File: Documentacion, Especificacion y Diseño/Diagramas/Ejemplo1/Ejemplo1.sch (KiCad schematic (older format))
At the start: 12 parts

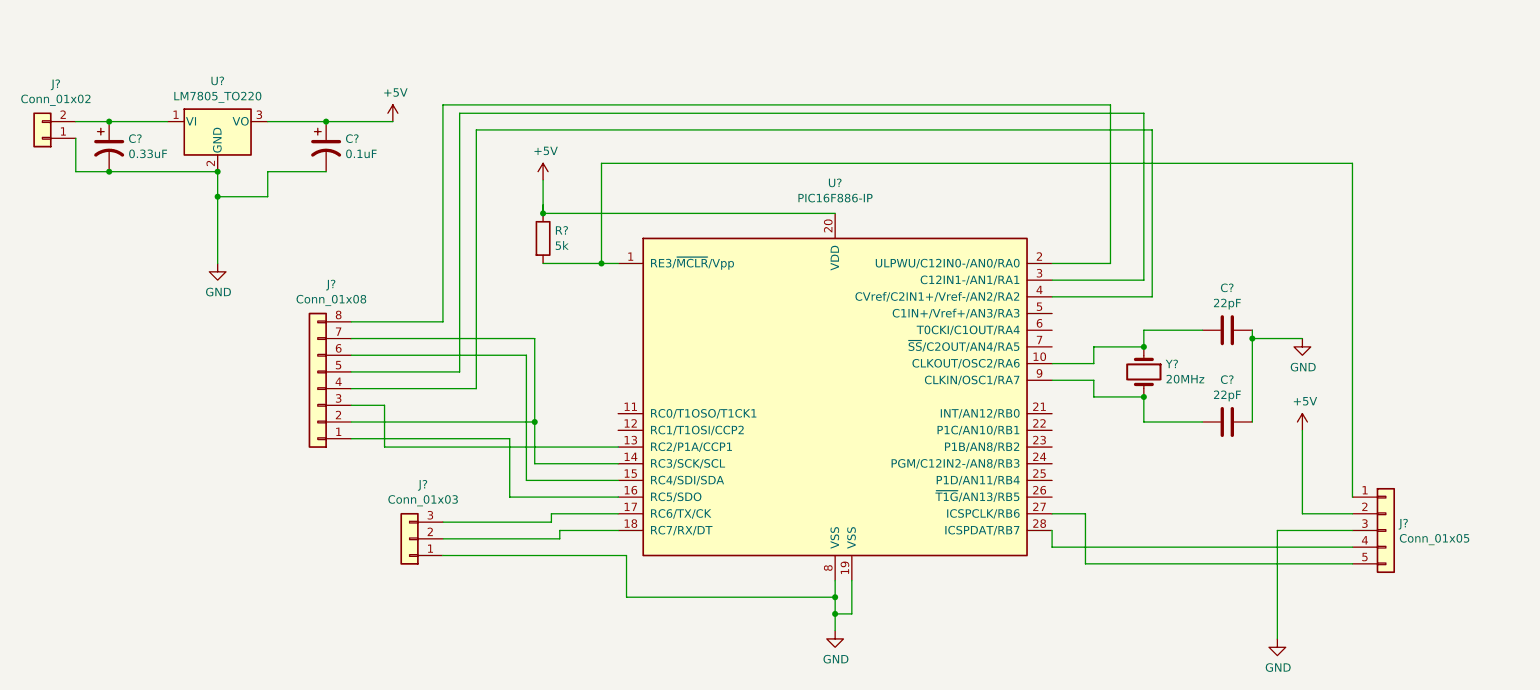
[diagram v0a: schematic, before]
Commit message: Tratado de hacer parte del circuito sin cruces y con especificaciones
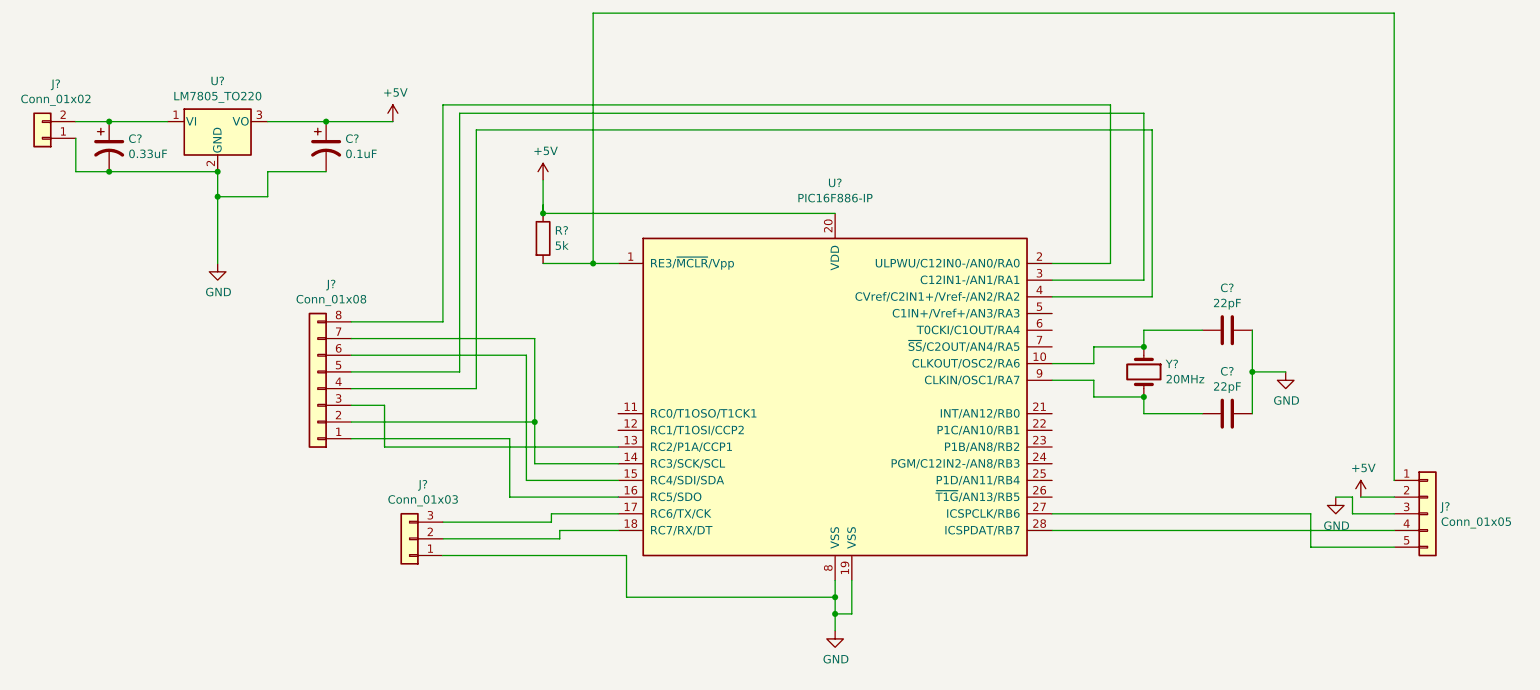
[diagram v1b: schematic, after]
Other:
- moved on the sheet: C?, J?
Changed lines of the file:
@@
 $EndComp
-Wire Wire Line
-	4000 2850 4350 2850
 Wire Wire Line
 	5750 2550 4000 2550
@@
 L Connector_Generic:Conn_01x05 J?
 U 1 1 635B6CD0
-P 9050 4450
-F 0 "J?" H 9130 4492 50  0000 L CNN
-F 1 "Conn_01x05" H 9130 4401 50  0000 L CNN
-F 2 "" H 9050 4450 50  0001 C CNN
-F 3 "~" H 9050 4450 50  0001 C CNN
-	1    9050 4450
+P 9300 4350
+F 0 "J?" H 9380 4392 50  0000 L CNN
+F 1 "Conn_01x05" H 9380 4301 50  0000 L CNN
+F 2 "" H 9300 4350 50  0001 C CNN
+F 3 "~" H 9300 4350 50  0001 C CNN
+	1    9300 4350
 	1    0    0    -1
 $EndComp
@@
 L power:+5V #PWR?
 U 1 1 635C3E4F
-P 8550 3850
-F 0 "#PWR?" H 8550 3700 50  0001 C CNN
-F 1 "+5V" H 8565 4023 50  0000 C CNN
-F 2 "" H 8550 3850 50  0001 C CNN
-F 3 "" H 8550 3850 50  0001 C CNN
-	1    8550 3850
+P 8900 4250
+F 0 "#PWR?" H 8900 4100 50  0001 C CNN
+F 1 "+5V" H 8915 4423 50  0000 C CNN
+F 2 "" H 8900 4250 50  0001 C CNN
+F 3 "" H 8900 4250 50  0001 C CNN
+	1    8900 4250
 	1    0    0    -1
 $EndComp
@@
 L power:GND #PWR?
 U 1 1 635C471C
-P 8400 5100
-F 0 "#PWR?" H 8400 4850 50  0001 C CNN
-F 1 "GND" H 8405 4927 50  0000 C CNN
-F 2 "" H 8400 5100 50  0001 C CNN
-F 3 "" H 8400 5100 50  0001 C CNN
-	1    8400 5100
-	1    0    0    -1
-$EndComp
-Wire Wire Line
-	8550 3850 8550 4350
-Wire Wire Line
-	8550 4350 8850 4350
-Wire Wire Line
-	8850 4450 8400 4450
-Wire Wire Line
-	8400 4450 8400 5100
-Wire Wire Line
-	8850 4250 8850 2250
-Wire Wire Line
-	8850 2250 4350 2250
-Wire Wire Line
-	4350 2250 4350 2850
-Connection ~ 4350 2850
-Wire Wire Line
-	4350 2850 4450 2850
-Wire Wire Line
-	8850 4550 7050 4550
-Wire Wire Line
-	7050 4550 7050 4450
-Wire Wire Line
-	8850 4650 7250 4650
-Wire Wire Line
-	7250 4650 7250 4350
-Wire Wire Line
-	7250 4350 7050 4350
+P 8750 4250
+F 0 "#PWR?" H 8750 4000 50  0001 C CNN
+F 1 "GND" H 8755 4077 50  0000 C CNN
+F 2 "" H 8750 4250 50  0001 C CNN
+F 3 "" H 8750 4250 50  0001 C CNN
+	1    8750 4250
+	1    0    0    -1
+$EndComp
 $Comp
 L Connector_Generic:Conn_01x03 J?
@@
 L Device:C C?
 U 1 1 635F47D1
-P 8100 3800
-F 0 "C?" V 7848 3800 50  0000 C CNN
-F 1 "22pF" V 7939 3800 50  0000 C CNN
-F 2 "" H 8138 3650 50  0001 C CNN
-F 3 "~" H 8100 3800 50  0001 C CNN
-	1    8100 3800
+P 8100 3750
+F 0 "C?" V 7848 3750 50  0000 C CNN
+F 1 "22pF" V 7939 3750 50  0000 C CNN
+F 2 "" H 8138 3600 50  0001 C CNN
+F 3 "~" H 8100 3750 50  0001 C CNN
+	1    8100 3750
 	0    1    1    0
 $EndComp
@@
 Wire Wire Line
 	7300 3550 7050 3550
+$Comp
+L power:GND #PWR?
+U 1 1 635FE965
+P 8450 3500
+F 0 "#PWR?" H 8450 3250 50  0001 C CNN
+F 1 "GND" H 8455 3327 50  0000 C CNN
+F 2 "" H 8450 3500 50  0001 C CNN
+F 3 "" H 8450 3500 50  0001 C CNN
+	1    8450 3500
+	1    0    0    -1
+$EndComp
 Wire Wire Line
 	7950 3250 7600 3250
@@
 Connection ~ 7600 3350
 Wire Wire Line
-	7950 3800 7600 3800
-Wire Wire Line
-	7600 3800 7600 3650
+	7950 3750 7600 3750
+Wire Wire Line
+	7600 3750 7600 3650
 Connection ~ 7600 3650
 Wire Wire Line
-	8250 3250 8250 3300
-$Comp
-L power:GND #PWR?
-U 1 1 635FE965
-P 8550 3300
-F 0 "#PWR?" H 8550 3050 50  0001 C CNN
-F 1 "GND" H 8555 3127 50  0000 C CNN
-F 2 "" H 8550 3300 50  0001 C CNN
-F 3 "" H 8550 3300 50  0001 C CNN
-	1    8550 3300
-	1    0    0    -1
-$EndComp
-Wire Wire Line
-	8550 3300 8250 3300
-Connection ~ 8250 3300
-Wire Wire Line
-	8250 3300 8250 3800
+	8250 3250 8250 3500
+Wire Wire Line
+	8450 3500 8250 3500
+Connection ~ 8250 3500
+Wire Wire Line
+	8250 3500 8250 3750
+Wire Wire Line
+	7050 4350 8600 4350
+Wire Wire Line
+	8600 4350 8600 4550
+Wire Wire Line
+	8600 4550 9100 4550
+Wire Wire Line
+	7050 4450 9100 4450
+Wire Wire Line
+	8750 4250 8850 4250
+Wire Wire Line
+	8850 4250 8850 4350
+Wire Wire Line
+	8850 4350 9100 4350
+Wire Wire Line
+	8900 4250 9100 4250
+Wire Wire Line
+	4000 2850 4300 2850
+Wire Wire Line
+	9100 4150 9100 1350
+Wire Wire Line
+	9100 1350 4300 1350
+Wire Wire Line
+	4300 1350 4300 2850
+Connection ~ 4300 2850
+Wire Wire Line
+	4300 2850 4450 2850
 $EndSCHEMATC
